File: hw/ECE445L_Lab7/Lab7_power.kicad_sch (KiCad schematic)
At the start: 15 parts, among them J1 2479774-1, SW1 SW_SPST, U1 LM2937ET-3.3_NOPB, U2 LM4041CILPR

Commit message: PCB Layout
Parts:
- added TP4: GND, ECE445L:Testpoint_1x02_P2.54mm, symbol ECE445L:Testpoint
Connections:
- net GND: now also TP4.1 (A), TP4.2 (B)
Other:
- note added: "Power Switch"
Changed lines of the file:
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@@
+		)
+	)
+	(text "Power Switch"
+		(exclude_from_sim no)
+		(at 166.37 25.4 0)
+		(effects
+			(font
+				(size 1.27 1.27)
+			)
 		)
 	)
@@
 	)
 	(junction
+		(at 154.305 51.435)
+		(diameter 0)
+		(color 0 0 0 0)
+	)
+	(junction
 		(at 174.625 35.56)
 		(diameter 0)
@@
 	)
 	(junction
+		(at 154.305 47.625)
+		(diameter 0)
+		(color 0 0 0 0)
+	)
+	(junction
 		(at 28.575 31.75)
 		(diameter 0)
@@
 	(wire
 		(pts
+			(xy 154.305 47.625) (xy 154.305 51.435)
+		)
+		(stroke
+			(width 0)
+			(type default)
+		)
+	)
+	(wire
+		(pts
 			(xy 248.92 126.365) (xy 248.92 130.175)
 		)
@@
 	(wire
 		(pts
+			(xy 154.305 51.435) (xy 154.305 52.705)
+		)
+		(stroke
+			(width 0)
+			(type default)
+		)
+	)
+	(wire
+		(pts
+			(xy 154.305 45.72) (xy 154.305 47.625)
+		)
+		(stroke
+			(width 0)
+			(type default)
+		)
+	)
+	(wire
+		(pts
 			(xy 28.575 31.75) (xy 28.575 34.925)
 		)
@@
 		(pts
 			(xy 78.74 31.75) (xy 78.74 34.925)
-		)
-		(stroke
-			(width 0)
-			(type default)
-		)
-	)
-	(wire
-		(pts
-			(xy 154.305 45.72) (xy 154.305 47.625)
 		)
 		(stroke
@@
 	(symbol
 		(lib_id "power:GND")
-		(at 154.305 47.625 0)
+		(at 154.305 52.705 0)
 		(unit 1)
 		(exclude_from_sim no)
@@
 		(dnp no)
 		(property "Reference" "#PWR07"
-			(at 154.305 53.975 0)
+			(at 154.305 59.055 0)
 			(effects
 				(font
@@
 		)
 		(property "Value" "GND"
-			(at 158.115 49.53 0)
+			(at 158.115 54.61 0)
 			(effects
 				(font
@@
 		)
 		(property "Footprint" ""
-			(at 154.305 47.625 0)
+			(at 154.305 52.705 0)
 			(effects
 				(font
@@
 		)
 		(property "Datasheet" ""
-			(at 154.305 47.625 0)
+			(at 154.305 52.705 0)
 			(effects
 				(font
@@
 		)
 		(property "Description" "Power symbol creates a global label with name \"GND\" , ground"
-			(at 154.305 47.625 0)
+			(at 154.305 52.705 0)
 			(effects
 				(font
@@
 					(unit 1)
 				)
+			)
+		)
+	)
+	(symbol
+		(lib_id "ECE445L:Testpoint")
+		(at 154.305 49.53 270)
+		(unit 1)
+		(exclude_from_sim no)
+		(in_bom yes)
+		(on_board yes)
+		(dnp no)
+		(property "Reference" "TP4"
+			(at 159.385 50.165 90)
+			(effects
+				(font
+					(size 1.27 1.27)
+				)
+				(justify left)
+			)
+		)
+		(property "Value" "GND"
+			(at 158.75 48.26 90)
+			(effects
+				(font
+					(size 1.27 1.27)
+				)
+				(justify left)
+			)
+		)
+		(property "Footprint" "ECE445L:Testpoint_1x02_P2.54mm"
+			(at 160.02 49.53 0)
+			(effects
+				(font
+					(size 1.27 1.27)
+				)
+				(hide yes)
+			)
+		)
+		(property "Datasheet" "~"
+			(at 154.305 49.53 0)
+			(effects
+				(font
+					(size 1.27 1.27)
+				)
+				(hide yes)
+			)
+		)
+		(property "Description" "Testpoint"
+			(at 154.305 49.53 0)
+			(effects
+				(font
+					(size 1.27 1.27)
+				)
+				(hide yes)
+			)
+		)
+		(pin "1"
+		)
+		(pin "2"
+		)
+		(instances
+			(project "ECE445L_Lab7"
+				(path "/69b823fd-c065-40ff-9bb9-c5835555f3eb/120cc903-6d6c-4a77-ad9c-c9f63dede169"
+					(reference "TP4")
+					(unit 1)
+				)

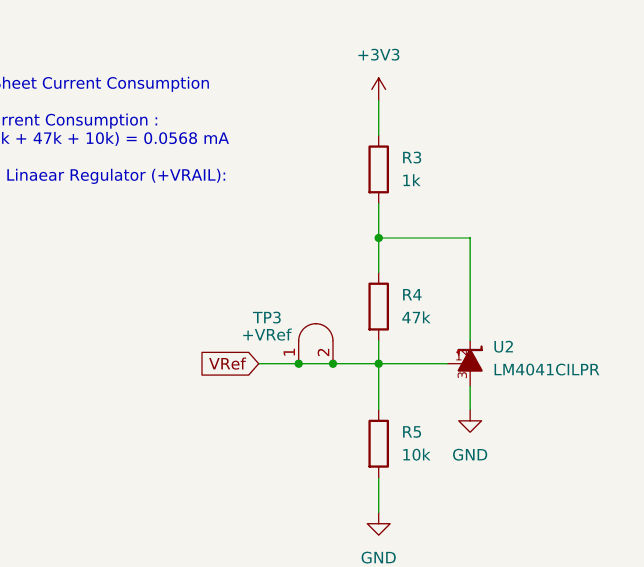
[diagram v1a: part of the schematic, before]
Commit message: Hardware layout - fixed voltage reference
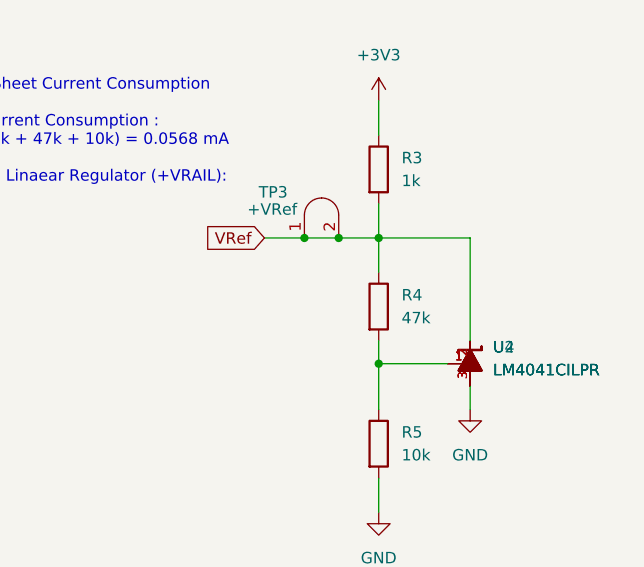
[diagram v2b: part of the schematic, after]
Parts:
- added U4: LM4041CILPR, ECE445L:ti_LM4041CILPR, symbol ti_LM4041CILPR:LM4041CILPR
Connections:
- net GND: now also U4.3
- net VRef: now also R3.2, R4.1, U2.2, U4.2; no longer R4.2, R5.1, U2.1
- new net: R4.2, R5.1, U2.1, U4.1
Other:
- moved on the sheet: TP3
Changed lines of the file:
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@@
+	)
+	(junction
+		(at 240.665 126.365)
+		(diameter 0)
+		(color 0 0 0 0)
 	)
 	(junction
@@
 	)
 	(junction
-		(at 243.84 140.335)
-		(diameter 0)
-		(color 0 0 0 0)
-	)
-	(junction
 		(at 182.88 35.56)
 		(diameter 0)
@@
 	)
 	(junction
-		(at 240.03 140.335)
+		(at 244.475 126.365)
 		(diameter 0)
 		(color 0 0 0 0)
@@
 	(wire
 		(pts
+			(xy 236.22 126.365) (xy 240.665 126.365)
+		)
+		(stroke
+			(width 0)
+			(type default)
+		)
+	)
+	(wire
+		(pts
 			(xy 248.92 111.125) (xy 248.92 114.935)
 		)
@@
 	(wire
 		(pts
-			(xy 259.08 126.365) (xy 248.92 126.365)
-		)
-		(stroke
-			(width 0)
-			(type default)
-		)
-	)
-	(wire
-		(pts
-			(xy 240.03 140.335) (xy 243.84 140.335)
-		)
-		(stroke
-			(width 0)
-			(type default)
-		)
-	)
-	(wire
-		(pts
 			(xy 78.74 31.75) (xy 74.295 31.75)
 		)
@@
 	(wire
 		(pts
-			(xy 235.585 140.335) (xy 240.03 140.335)
-		)
-		(stroke
-			(width 0)
-			(type default)
-		)
-	)
-	(wire
-		(pts
 			(xy 140.335 45.72) (xy 154.305 45.72)
 		)
@@
 	(wire
 		(pts
+			(xy 240.665 126.365) (xy 244.475 126.365)
+		)
+		(stroke
+			(width 0)
+			(type default)
+		)
+	)
+	(wire
+		(pts
 			(xy 154.305 38.1) (xy 154.305 40.64)
 		)
@@
 	(wire
 		(pts
-			(xy 243.84 140.335) (xy 248.92 140.335)
-		)
-		(stroke
-			(width 0)
-			(type default)
-		)
-	)
-	(wire
-		(pts
 			(xy 248.92 122.555) (xy 248.92 126.365)
 		)
@@
 	(wire
 		(pts
+			(xy 244.475 126.365) (xy 248.92 126.365)
+		)
+		(stroke
+			(width 0)
+			(type default)
+		)
+	)
+	(wire
+		(pts
 			(xy 28.575 31.75) (xy 35.56 31.75)
 		)
@@
 		(pts
 			(xy 73.66 43.815) (xy 78.74 43.815)
+		)
+		(stroke
+			(width 0)
+			(type default)
+		)
+	)
+	(wire
+		(pts
+			(xy 248.92 126.365) (xy 259.08 126.365)
 		)
 		(stroke
@@
 	(global_label "VRef"
 		(shape input)
-		(at 235.585 140.335 180)
+		(at 236.22 126.365 180)
 		(fields_autoplaced yes)
 		(effects
@@
 		)
 		(property "Intersheetrefs" "${INTERSHEET_REFS}"
-			(at 228.4269 140.335 0)
+			(at 229.0619 126.365 0)
 			(effects
 				(font
@@
 	(symbol
 		(lib_id "ECE445L:Testpoint")
-		(at 241.935 140.335 0)
+		(at 242.57 126.365 0)
 		(unit 1)
 		(exclude_from_sim no)
@@
 		(dnp no)
 		(property "Reference" "TP3"
-			(at 234.95 135.255 0)
+			(at 235.585 121.285 0)
 			(effects
 				(font
@@
 		)
 		(property "Value" "+VRef"
-			(at 233.68 137.16 0)
+			(at 234.315 123.19 0)
 			(effects
 				(font
@@
 		)
 		(property "Footprint" "ECE445L:Testpoint_1x02_P2.54mm"
-			(at 241.935 134.62 0)
+			(at 242.57 120.65 0)
 			(effects
 				(font
@@
 		)
 		(property "Datasheet" "~"
-			(at 241.935 140.335 0)
+			(at 242.57 126.365 0)
 			(effects
 				(font
@@
 		)
 		(property "Description" "Testpoint"
-			(at 241.935 140.335 0)
+			(at 242.57 126.365 0)
 			(effects
 				(font
@@
 					(unit 1)
 				)
+			)
+		)
+	)
+	(symbol
+		(lib_id "ti_LM4041CILPR:LM4041CILPR")
+		(at 259.08 140.335 0)
+		(unit 1)
+		(exclude_from_sim no)
+		(in_bom yes)
+		(on_board yes)
+		(dnp no)
+		(fields_autoplaced yes)
+		(property "Reference" "U4"
+			(at 261.62 138.4934 0)
+			(effects
+				(font
+					(size 1.27 1.27)
+				)
+				(justify left)
+			)
+		)
+		(property "Value" "LM4041CILPR"
+			(at 261.62 141.0334 0)
+			(effects
+				(font
+					(size 1.27 1.27)
+				)
+				(justify left)
+			)
+		)
+		(property "Footprint" "ECE445L:ti_LM4041CILPR"
+			(at 259.08 140.335 0)
+			(effects
+				(font
+					(size 1.27 1.27)
+				)
+				(justify bottom)
+				(hide yes)
+			)
+		)
+		(property "Datasheet" "https://www.ti.com/general/docs/suppproductinfo.tsp?distId=26&gotoUrl=https://www.ti.com/lit/gpn/lm4041a12"
+			(at 259.08 140.335 0)
+			(effects
+				(font
+					(size 1.27 1.27)
+				)
+				(hide yes)
+			)
+		)
+		(property "Description" ""
+			(at 259.08 140.335 0)
+			(effects
+				(font
+					(size 1.27 1.27)
+				)
+				(hide yes)
+			)
+		)
+		(property "Distributor" "Mouser"
+			(at 259.08 140.335 0)
+			(effects
+				(font
+					(size 1.27 1.27)
+				)
+				(hide yes)
+			)
+		)
+		(property "Manufacturer" "Texas Instruments"
+			(at 259.08 140.335 0)
+			(effects
+				(font
+					(size 1.27 1.27)
+				)
+				(hide yes)
+			)
+		)
+		(property "P/N" "LM4041CILPR"
+			(at 259.08 140.335 0)
+			(effects
+				(font
+					(size 1.27 1.27)
+				)
+				(hide yes)
+			)
+		)
+		(property "LCSC Part #" ""
+			(at 259.08 140.335 0)
+			(effects
+				(font
+					(size 1.27 1.27)
+				)
+				(hide yes)
+			)
+		)
+		(property "Cost" "0.78"
+			(at 259.08 140.335 0)
+			(effects
+				(font
+					(size 1.27 1.27)
+				)
+				(hide yes)
+			)
+		)
+		(pin "2"
+		)
+		(pin "1"
+		)
+		(pin "3"
+		)
+		(instances
+			(project "ECE445L_Lab7"
+				(path "/69b823fd-c065-40ff-9bb9-c5835555f3eb/120cc903-6d6c-4a77-ad9c-c9f63dede169"
+					(reference "U4")
+					(unit 1)
+				)

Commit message: Pushing so i can work on my desktop
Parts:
- removed U4: LM4041CILPR, ECE445L:ti_LM4041CILPR, symbol ti_LM4041CILPR:LM4041CILPR
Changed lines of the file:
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@@
-	)
-	(symbol
-		(lib_id "ti_LM4041CILPR:LM4041CILPR")
-		(at 259.08 140.335 0)
-		(unit 1)
-		(exclude_from_sim no)
-		(in_bom yes)
-		(on_board yes)
-		(dnp no)
-		(fields_autoplaced yes)
-		(property "Reference" "U4"
-			(at 261.62 138.4934 0)
-			(effects
-				(font
-					(size 1.27 1.27)
-				)
-				(justify left)
-			)
-		)
-		(property "Value" "LM4041CILPR"
-			(at 261.62 141.0334 0)
-			(effects
-				(font
-					(size 1.27 1.27)
-				)
-				(justify left)
-			)
-		)
-		(property "Footprint" "ECE445L:ti_LM4041CILPR"
-			(at 259.08 140.335 0)
-			(effects
-				(font
-					(size 1.27 1.27)
-				)
-				(justify bottom)
-				(hide yes)
-			)
-		)
-		(property "Datasheet" "https://www.ti.com/general/docs/suppproductinfo.tsp?distId=26&gotoUrl=https://www.ti.com/lit/gpn/lm4041a12"
-			(at 259.08 140.335 0)
-			(effects
-				(font
-					(size 1.27 1.27)
-				)
-				(hide yes)
-			)
-		)
-		(property "Description" ""
-			(at 259.08 140.335 0)
-			(effects
-				(font
-					(size 1.27 1.27)
-				)
-				(hide yes)
-			)
-		)
-		(property "Distributor" "Mouser"
-			(at 259.08 140.335 0)
-			(effects
-				(font
-					(size 1.27 1.27)
-				)
-				(hide yes)
-			)
-		)
-		(property "Manufacturer" "Texas Instruments"
-			(at 259.08 140.335 0)
-			(effects
-				(font
-					(size 1.27 1.27)
-				)
-				(hide yes)
-			)
-		)
-		(property "P/N" "LM4041CILPR"
-			(at 259.08 140.335 0)
-			(effects
-				(font
-					(size 1.27 1.27)
-				)
-				(hide yes)
-			)
-		)
-		(property "LCSC Part #" ""
-			(at 259.08 140.335 0)
-			(effects
-				(font
-					(size 1.27 1.27)
-				)
-				(hide yes)
-			)
-		)
-		(property "Cost" "0.78"
-			(at 259.08 140.335 0)
-			(effects
-				(font
-					(size 1.27 1.27)
-				)
-				(hide yes)
-			)
-		)
-		(pin "2"
-		)
-		(pin "1"
-		)
-		(pin "3"
-		)
-		(instances
-			(project "ECE445L_Lab7"
-				(path "/69b823fd-c065-40ff-9bb9-c5835555f3eb/120cc903-6d6c-4a77-ad9c-c9f63dede169"
-					(reference "U4")
-					(unit 1)
-				)
-			)
-		)
 	)
 	(symbol

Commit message: Final PCB commit
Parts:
- added TP1: +3V3, ECE445L:Testpoint_1x02_P2.54mm, symbol ECE445L:Testpoint
- added TP4: GND, ECE445L:Testpoint_1x02_P2.54mm, symbol ECE445L:Testpoint
- SW1: symbol Switch:SW_SPST -> ECE445L:Power_Switch
- TP2: renamed from TP1; value 3V3 -> +3V3
- renumbered TP4 to TP3, TP2 to TP5, TP3 to TP6
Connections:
- net +3V3: now also TP1.1 (A), TP1.2 (B)
- net GND: now also TP4.1 (A), TP4.2 (B)
